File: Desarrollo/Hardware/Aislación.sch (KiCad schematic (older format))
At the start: 28 parts, among them U11 ADuM6401, U12 ADuM2401, U13 NCP1117ST33T3G

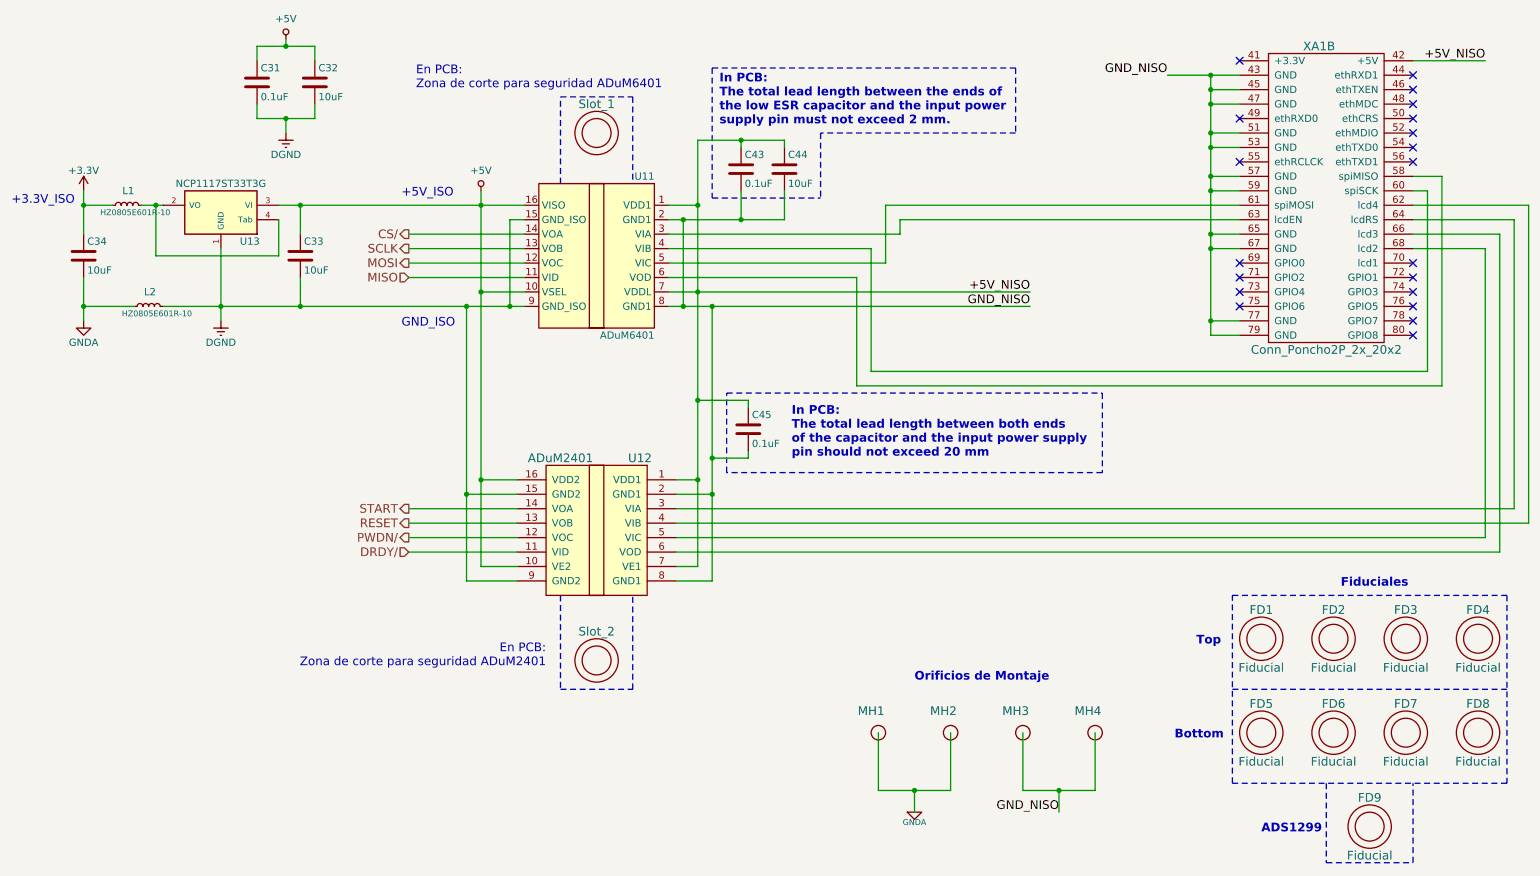
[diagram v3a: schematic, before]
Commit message: Actualización de PCB. Cotas de diseño. Generación de BOM. Archivos Gerber disponibles en carpeta "gerbers". Colocación de eje auxiliar de posicionamiento en mounting hole inferior izquierdo. Actualización de esquemático con modificación de comentarios y adición de código de compra DigiKey y hoja de datos en algunos componentes que faltaban. FINALIZADO
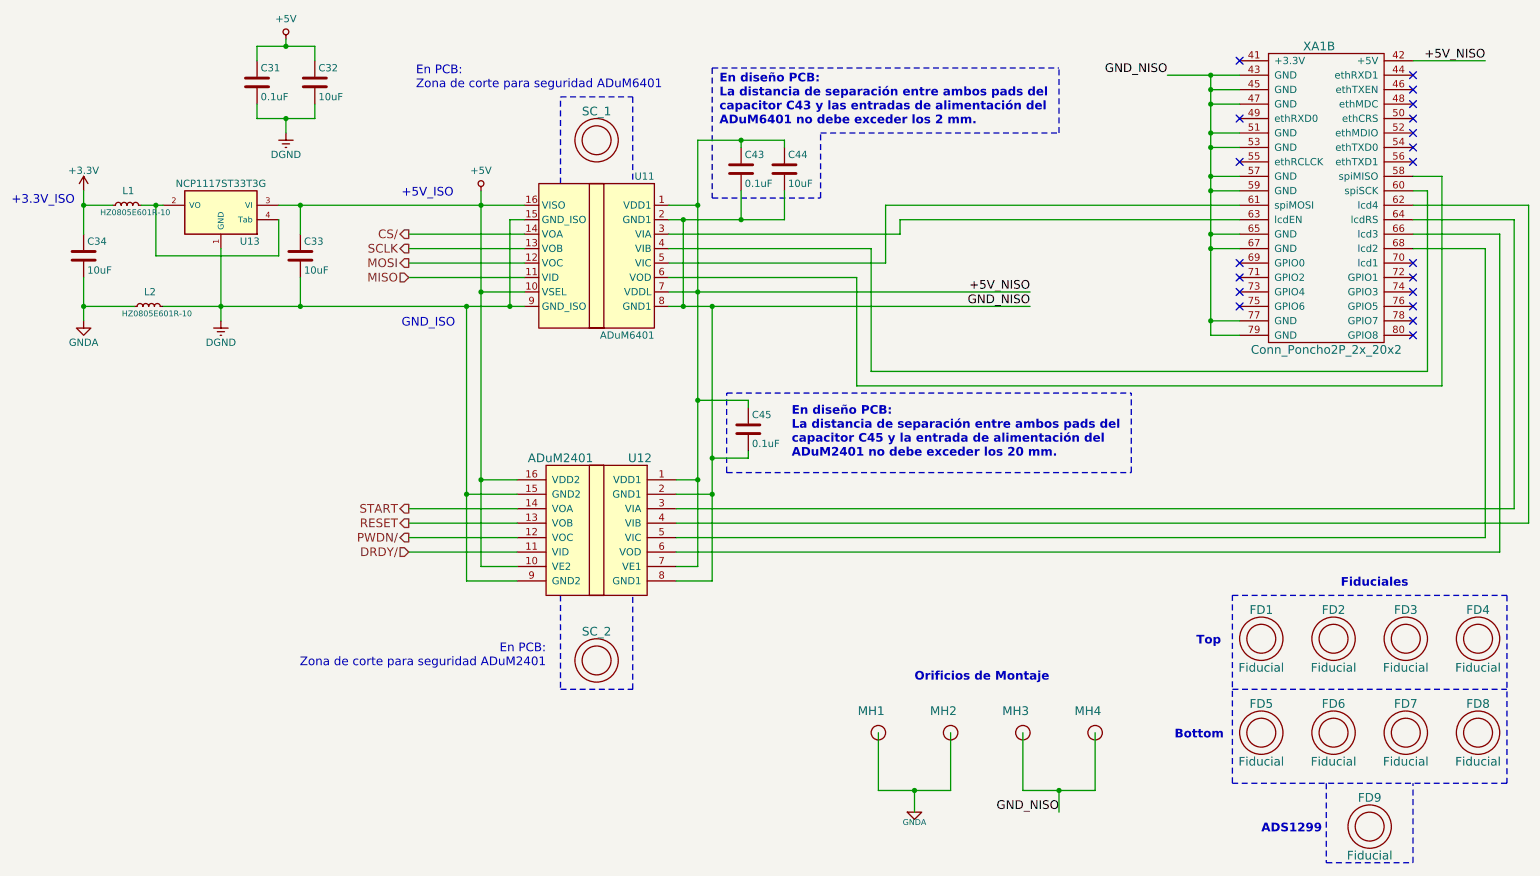
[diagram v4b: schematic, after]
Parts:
- removed Slot_1: Fiducial, Fiducials:Fiducial_1mm_Dia_2.54mm_Outer_CopperTop, symbol Fiducial
- added SC_1: Slot_1, Fiducials:Fiducial_1mm_Dia_2.54mm_Outer_CopperTop, symbol Fiducial
- C43, C45: Código Digikey (none) -> 399-1170-1-ND
- C44: Código Digikey (none) -> 399-8012-1-ND
- XA1: Código Digikey S7123-ND -> S2011EC-20-ND
- renumbered Slot_2 to SC_2
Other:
- note added: "En diseño PCB:\nLa distancia de separación entre ambos pads del\ncapacitor C43 y las entradas de alimentación del\nADuM6401 no debe exceder los 2 mm."
- note added: "En diseño PCB:\nLa distancia de separación entre ambos pads del\ncapacitor C45 y la entrada de alimentación del\nADuM2401 no debe exceder los 20 mm."
- note removed: "In PCB:\nThe total lead length between both ends\nof the capacitor and the input power supply\npin should not exceed 20 mm"
- note removed: "In PCB:\nThe total lead length between the ends of\nthe low ESR capacitor and the input power\nsupply pin must not exceed 2 mm."
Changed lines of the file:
@@
 F 1 "Conn_Poncho2P_2x_20x2" H 9650 -500 60  0000 C CNN
 F 2 "Poncho_Esqueleto:Conn_Poncho_Izquierdo" H 9300 1200 60  0001 C CNN
-F 3 "http://www.sullinscorp.com/drawings/78_P(N)PxCxxxLFBN-RC,_10492-H.pdf" H 9300 1200 60  0001 C CNN
-F 4 "S7123-ND" H 9300 1200 60  0001 C CNN "Código Digikey"
+F 3 "https://media.digikey.com/PDF/Data%20Sheets/Sullins%20PDFs/xRxCzzzDxxN-RC_11636-B.pdf" H 9300 1200 60  0001 C CNN
+F 4 "S2011EC-20-ND" H 9300 1200 60  0001 C CNN "Código Digikey"
 	2    9300 1200
 	1    0    0    -1
@@
 F 2 "Capacitors_SMD:C_0805" H 5638 1500 50  0001 C CNN
 F 3 "http://www.kemet.com/Lists/ProductCatalog/Attachments/19/KEM_C1006_X5R_SMD.pdf" H 5600 1650 50  0001 C CNN
+F 4 "399-1170-1-ND" H 5600 1650 60  0001 C CNN "Código Digikey"
 	1    5600 1650
 	1    0    0    -1
@@
 F 2 "Capacitors_SMD:C_0805" H 5938 1500 50  0001 C CNN
 F 3 "http://www.kemet.com/Lists/ProductCatalog/Attachments/19/KEM_C1006_X5R_SMD.pdf" H 5900 1650 50  0001 C CNN
+F 4 "399-8012-1-ND" H 5900 1650 60  0001 C CNN "Código Digikey"
 	1    5900 1650
 	1    0    0    -1
@@
 F 2 "Capacitors_SMD:C_0805" H 5688 3300 50  0001 C CNN
 F 3 "http://www.kemet.com/Lists/ProductCatalog/Attachments/19/KEM_C1006_X5R_SMD.pdf" H 5650 3450 50  0001 C CNN
+F 4 "399-1170-1-ND" H 5650 3450 60  0001 C CNN "Código Digikey"
 	1    5650 3450
 	1    0    0    -1
@@
 F 1 "Fiducial" H 9200 4700 60  0000 C CNN
 F 2 "Fiducials:Fiducial_1mm_Dia_2.54mm_Outer_CopperTop" H 9200 4900 60  0001 C CNN
-F 3 "" H 9200 4900 60  0000 C CNN
+F 3 "NONE" H 9200 4900 60  0001 C CNN
 	1    9200 4900
 	1    0    0    -1
@@
 F 1 "Fiducial" H 9700 4700 60  0000 C CNN
 F 2 "Fiducials:Fiducial_1mm_Dia_2.54mm_Outer_CopperTop" H 9700 4900 60  0001 C CNN
-F 3 "" H 9700 4900 60  0000 C CNN
+F 3 "NONE" H 9700 4900 60  0001 C CNN
 	1    9700 4900
 	1    0    0    -1
@@
 F 1 "Fiducial" H 10200 4700 60  0000 C CNN
 F 2 "Fiducials:Fiducial_1mm_Dia_2.54mm_Outer_CopperTop" H 10200 4900 60  0001 C CNN
-F 3 "" H 10200 4900 60  0000 C CNN
+F 3 "NONE" H 10200 4900 60  0001 C CNN
 	1    10200 4900
 	1    0    0    -1
@@
 F 1 "Fiducial" H 10700 4700 60  0000 C CNN
 F 2 "Fiducials:Fiducial_1mm_Dia_2.54mm_Outer_CopperTop" H 10700 4900 60  0001 C CNN
-F 3 "" H 10700 4900 60  0000 C CNN
+F 3 "NONE" H 10700 4900 60  0001 C CNN
 	1    10700 4900
 	1    0    0    -1
@@
 F 1 "PCB_HOLE" H 7050 5450 60  0001 C CNN
 F 2 "Connect:1pin" H 6900 5600 60  0001 C CNN
-F 3 "PCB HOLE" H 7000 5700 60  0001 C CNN
+F 3 "NONE" H 7000 5700 60  0001 C CNN
 	1    7050 5550
 	1    0    0    -1
@@
 F 1 "PCB_HOLE" H 7550 5450 60  0001 C CNN
 F 2 "Connect:1pin" H 7400 5600 60  0001 C CNN
-F 3 "PCB HOLE" H 7500 5700 60  0001 C CNN
+F 3 "NONE" H 7500 5700 60  0001 C CNN
 	1    7550 5550
 	1    0    0    -1
@@
 F 1 "PCB_HOLE" H 8050 5450 60  0001 C CNN
 F 2 "Connect:1pin" H 7900 5600 60  0001 C CNN
-F 3 "PCB HOLE" H 8000 5700 60  0001 C CNN
+F 3 "NONE" H 8000 5700 60  0001 C CNN
 	1    8050 5550
 	1    0    0    -1
@@
 F 1 "PCB_HOLE" H 6550 5450 60  0001 C CNN
 F 2 "Connect:1pin" H 6400 5600 60  0001 C CNN
-F 3 "PCB HOLE" H 6500 5700 60  0001 C CNN
+F 3 "NONE" H 6500 5700 60  0001 C CNN
 	1    6550 5550
 	1    0    0    -1
@@
 F 1 "Fiducial" H 9950 6000 60  0000 C CNN
 F 2 "Fiducials:Fiducial_1mm_Dia_2.54mm_Outer_CopperTop" H 9950 6200 60  0001 C CNN
-F 3 "" H 9950 6200 60  0000 C CNN
+F 3 "NONE" H 9950 6200 60  0001 C CNN
 	1    9950 6200
 	1    0    0    -1
@@
 F 1 "Fiducial" H 9200 5350 60  0000 C CNN
 F 2 "Fiducials:Fiducial_1mm_Dia_2.54mm_Outer_CopperTop" H 9200 5550 60  0001 C CNN
-F 3 "" H 9200 5550 60  0000 C CNN
+F 3 "NONE" H 9200 5550 60  0001 C CNN
 	1    9200 5550
 	1    0    0    -1
@@
 F 1 "Fiducial" H 9700 5350 60  0000 C CNN
 F 2 "Fiducials:Fiducial_1mm_Dia_2.54mm_Outer_CopperTop" H 9700 5550 60  0001 C CNN
-F 3 "" H 9700 5550 60  0000 C CNN
+F 3 "NONE" H 9700 5550 60  0001 C CNN
 	1    9700 5550
 	1    0    0    -1
@@
 F 1 "Fiducial" H 10200 5350 60  0000 C CNN
 F 2 "Fiducials:Fiducial_1mm_Dia_2.54mm_Outer_CopperTop" H 10200 5550 60  0001 C CNN
-F 3 "" H 10200 5550 60  0000 C CNN
+F 3 "NONE" H 10200 5550 60  0001 C CNN
 	1    10200 5550
 	1    0    0    -1
@@
 F 1 "Fiducial" H 10700 5350 60  0000 C CNN
 F 2 "Fiducials:Fiducial_1mm_Dia_2.54mm_Outer_CopperTop" H 10700 5550 60  0001 C CNN
-F 3 "" H 10700 5550 60  0000 C CNN
+F 3 "NONE" H 10700 5550 60  0001 C CNN
 	1    10700 5550
 	1    0    0    -1
@@
 $EndComp
 $Comp
-L Fiducial Slot_1
-U 1 1 5813B1F6
-P 4600 1400
-F 0 "Slot_1" H 4600 1600 60  0000 C CNN
-F 1 "Fiducial" H 4600 1200 60  0001 C CNN
-F 2 "Fiducials:Fiducial_1mm_Dia_2.54mm_Outer_CopperTop" H 4600 1400 60  0001 C CNN
-F 3 "" H 4600 1400 60  0000 C CNN
-	1    4600 1400
-	1    0    0    -1
-$EndComp
-$Comp
-L Fiducial Slot_2
+L Fiducial SC_2
 U 1 1 5813B95D
 P 4600 5050
-F 0 "Slot_2" H 4600 5250 60  0000 C CNN
+F 0 "SC_2" H 4600 5250 60  0000 C CNN
 F 1 "Slot_2" H 4600 4850 60  0001 C CNN
 F 2 "Fiducials:Fiducial_1mm_Dia_2.54mm_Outer_CopperTop" H 4600 5050 60  0001 C CNN
-F 3 "" H 4600 5050 60  0000 C CNN
+F 3 "NONE" H 4600 5050 60  0001 C CNN
 	1    4600 5050
 	1    0    0    -1
 $EndComp
-Text Notes 5950 3650 0    60   ~ 12
-In PCB:\nThe total lead length between both ends\nof the capacitor and the input power supply\npin should not exceed 20 mm
 Wire Notes Line
 	5400 1850 6150 1850
 Wire Notes Line
-	5400 950  7500 950
-Wire Notes Line
-	7500 950  7500 1400
+	5400 950  7800 950
 Wire Notes Line
 	5400 950  5400 1850
 Wire Notes Line
-	7500 1400 6150 1400
-Wire Notes Line
-	6150 1400 6150 1850
+	6150 1400 7800 1400
+Wire Notes Line
+	6150 1850 6150 1400
 Text Notes 5450 1350 0    60   ~ 12
-In PCB:\nThe total lead length between the ends of\nthe low ESR capacitor and the input power\nsupply pin must not exceed 2 mm.
-Wire Notes Line
-	5500 3200 8100 3200
-Wire Notes Line
-	8100 3200 8100 3750
-Wire Notes Line
-	8100 3750 5500 3750
+En diseño PCB:\nLa distancia de separación entre ambos pads del\ncapacitor C43 y las entradas de alimentación del\nADuM6401 no debe exceder los 2 mm.
+Wire Notes Line
+	5500 3200 8300 3200
+Wire Notes Line
+	5500 3750 8300 3750
 Wire Notes Line
 	5500 3750 5500 3200
@@
 Wire Notes Line
 	4850 5250 4850 4600
+$Comp
+L Fiducial SC_1
+U 1 1 58163B71
+P 4600 1450
+F 0 "SC_1" H 4600 1650 60  0000 C CNN
+F 1 "Slot_1" H 4600 1250 60  0001 C CNN
+F 2 "Fiducials:Fiducial_1mm_Dia_2.54mm_Outer_CopperTop" H 4600 1450 60  0001 C CNN
+F 3 "NONE" H 4600 1450 60  0001 C CNN
+	1    4600 1450
+	1    0    0    -1
+$EndComp
+Wire Notes Line
+	7800 1400 7800 950
+Text Notes 5950 3650 0    60   ~ 12
+En diseño PCB:\nLa distancia de separación entre ambos pads del\ncapacitor C45 y la entrada de alimentación del\nADuM2401 no debe exceder los 20 mm.
+Wire Notes Line
+	8300 3750 8300 3200
 $EndSCHEMATC

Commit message: Actualización de propiedades de 4 componentes en esquemático "Aislación.sch" y correspondiente generación de nueva BOM.
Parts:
- C31: Código Digikey (none) -> 399-1170-1-ND
- C32, C33, C34: Código Digikey (none) -> 399-8012-1-ND
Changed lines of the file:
@@
 F 2 "Capacitors_SMD:C_0805" H 2588 2100 50  0001 C CNN
 F 3 "http://www.kemet.com/Lists/ProductCatalog/Attachments/19/KEM_C1006_X5R_SMD.pdf" H 2550 2250 50  0001 C CNN
+F 4 "399-8012-1-ND" H 2550 2250 60  0001 C CNN "Código Digikey"
 	1    2550 2250
 	1    0    0    -1
@@
 F 2 "Capacitors_SMD:C_0805" H 1088 2100 50  0001 C CNN
 F 3 "http://www.kemet.com/Lists/ProductCatalog/Attachments/19/KEM_C1006_X5R_SMD.pdf" H 1050 2250 50  0001 C CNN
+F 4 "399-8012-1-ND" H 1050 2250 60  0001 C CNN "Código Digikey"
 	1    1050 2250
 	1    0    0    -1
@@
 F 2 "Capacitors_SMD:C_0805" H 2288 900 50  0001 C CNN
 F 3 "http://www.kemet.com/Lists/ProductCatalog/Attachments/53/KEM_C1002_X7R_SMD.pdf" H 2250 1050 50  0001 C CNN
+F 4 "399-1170-1-ND" H 2250 1050 60  0001 C CNN "Código Digikey"
 	1    2250 1050
 	1    0    0    -1
@@
 F 2 "Capacitors_SMD:C_0805" H 2688 900 50  0001 C CNN
 F 3 "http://www.kemet.com/Lists/ProductCatalog/Attachments/19/KEM_C1006_X5R_SMD.pdf" H 2650 1050 50  0001 C CNN
+F 4 "399-8012-1-ND" H 2650 1050 60  0001 C CNN "Código Digikey"
 	1    2650 1050
 	1    0    0    -1
